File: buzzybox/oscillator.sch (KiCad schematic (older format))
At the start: 6 parts, among them Q1 Q_NPN_EBC

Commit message: complete mini layout
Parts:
- removed C2: C, Capacitor_THT:CP_Radial_D5.0mm_P2.50mm, symbol Device:C
- added C10: CP1, Capacitor_THT:CP_Radial_D4.0mm_P2.00mm, symbol Device:CP1
- Q1: value Q_NPN_EBC -> NPN
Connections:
- net at Q1.1 (E), R2.2, RV1.3: now also C10.1
- net at D1.2 (A), Q1.3 (C): now also C10.2
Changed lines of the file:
@@
 AR Path="/5FD4298B/5FB07025" Ref="Q14"  Part="1"
 F 0 "Q5" H 5641 3804 50  0000 L CNN
-F 1 "Q_NPN_EBC" H 5641 3895 50  0000 L CNN
+F 1 "NPN" H 5641 3895 50  0000 L CNN
 F 2 "buzzybox:TO-92-2" H 5650 3950 50  0001 C CNN
 F 3 "~" H 5450 3850 50  0001 C CNN
@@
 Wire Wire Line
 	5600 3550 5600 3650
-$Comp
-L Device:C C?
-U 1 1 5FB0704B
-P 5850 3850
-AR Path="/5FB0704B" Ref="C?"  Part="1"
-AR Path="/5FB04F5B/5FB0704B" Ref="C?"  Part="1"
-AR Path="/5FB0809B/5FB0704B" Ref="C?"  Part="1"
-AR Path="/5FB08189/5FB0704B" Ref="C?"  Part="1"
-AR Path="/5FB0823D/5FB0704B" Ref="C?"  Part="1"
-AR Path="/5FB0838F/5FB0704B" Ref="C?"  Part="1"
-AR Path="/5FB083E3/5FB0704B" Ref="C?"  Part="1"
-AR Path="/5FB084BD/5FB0704B" Ref="C?"  Part="1"
-AR Path="/5FB1B762/5FB0704B" Ref="C?"  Part="1"
-AR Path="/5FB1B962/5FB0704B" Ref="C?"  Part="1"
-AR Path="/5FB1BC8A/5FB0704B" Ref="C?"  Part="1"
-AR Path="/5FB1BF2A/5FB0704B" Ref="C?"  Part="1"
-AR Path="/5FB1C1D8/5FB0704B" Ref="C?"  Part="1"
-AR Path="/5FB1C552/5FB0704B" Ref="C?"  Part="1"
-AR Path="/5FD40CD3/5FB0704B" Ref="C2"  Part="1"
-AR Path="/5FD412A5/5FB0704B" Ref="C3"  Part="1"
-AR Path="/5FD41369/5FB0704B" Ref="C4"  Part="1"
-AR Path="/5FD41435/5FB0704B" Ref="C5"  Part="1"
-AR Path="/5FD4152B/5FB0704B" Ref="C6"  Part="1"
-AR Path="/5FD41635/5FB0704B" Ref="C7"  Part="1"
-AR Path="/5FD416C9/5FB0704B" Ref="C8"  Part="1"
-AR Path="/5FD42979/5FB0704B" Ref="C9"  Part="1"
-AR Path="/5FD4297C/5FB0704B" Ref="C10"  Part="1"
-AR Path="/5FD4297F/5FB0704B" Ref="C11"  Part="1"
-AR Path="/5FD42982/5FB0704B" Ref="C12"  Part="1"
-AR Path="/5FD42985/5FB0704B" Ref="C13"  Part="1"
-AR Path="/5FD42988/5FB0704B" Ref="C14"  Part="1"
-AR Path="/5FD4298B/5FB0704B" Ref="C15"  Part="1"
-F 0 "C6" H 5965 3896 50  0000 L CNN
-F 1 "C" H 5965 3805 50  0000 L CNN
-F 2 "Capacitor_THT:CP_Radial_D5.0mm_P2.50mm" H 5888 3700 50  0001 C CNN
-F 3 "~" H 5850 3850 50  0001 C CNN
-	1    5850 3850
-	1    0    0    -1
-$EndComp
 Wire Wire Line
 	5850 4050 5850 4000
@@
 	-1   0    0    1
 $EndComp
+$Comp
+L Device:CP1 C10
+U 1 1 5FD88ECD
+P 5850 3850
+AR Path="/5FD4297F/5FD88ECD" Ref="C10"  Part="1"
+AR Path="/5FD40CD3/5FD88ECD" Ref="C1"  Part="1"
+AR Path="/5FD412A5/5FD88ECD" Ref="C2"  Part="1"
+AR Path="/5FD41369/5FD88ECD" Ref="C3"  Part="1"
+AR Path="/5FD41435/5FD88ECD" Ref="C4"  Part="1"
+AR Path="/5FD4152B/5FD88ECD" Ref="C5"  Part="1"
+AR Path="/5FD41635/5FD88ECD" Ref="C6"  Part="1"
+AR Path="/5FD416C9/5FD88ECD" Ref="C7"  Part="1"
+AR Path="/5FD42979/5FD88ECD" Ref="C8"  Part="1"
+AR Path="/5FD4297C/5FD88ECD" Ref="C9"  Part="1"
+F 0 "C5" H 5965 3896 50  0000 L CNN
+F 1 "CP1" H 5965 3805 50  0000 L CNN
+F 2 "Capacitor_THT:CP_Radial_D4.0mm_P2.00mm" H 5850 3850 50  0001 C CNN
+F 3 "~" H 5850 3850 50  0001 C CNN
+	1    5850 3850
+	1    0    0    -1
+$EndComp
 $EndSCHEMATC

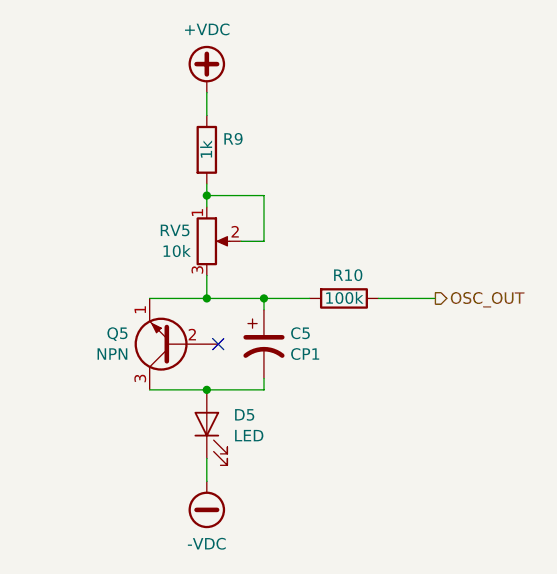
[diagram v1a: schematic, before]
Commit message: finalize main PCB after parts recieved
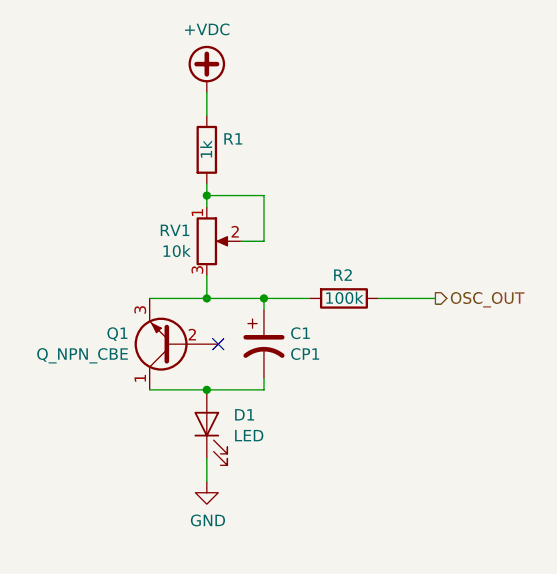
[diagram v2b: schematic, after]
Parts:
- removed Q1: NPN, buzzybox:TO-92-2, symbol Device:Q_NPN_EBC
- added Q1: Q_NPN_CBE, buzzybox:TO-92-2, symbol Device:Q_NPN_CBE
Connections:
- net at C10.1, R2.2, RV1.3: now also Q1.3 (E)
- net at C10.2, D1.2 (A): now also Q1.1 (C)
- net -VDC renamed GND
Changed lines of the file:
@@
 $Descr A4 11693 8268
 encoding utf-8
-Sheet 6 11
+Sheet 2 11
 Title ""
 Date ""
@@
 AR Path="/5FD42988/5FB07013" Ref="R25"  Part="1"
 AR Path="/5FD4298B/5FB07013" Ref="R27"  Part="1"
-F 0 "R9" H 5670 3046 50  0000 L CNN
+F 0 "R1" H 5670 3046 50  0000 L CNN
 F 1 "1k" V 5600 3000 50  0000 C CNN
 F 2 "Resistor_THT:R_Axial_DIN0207_L6.3mm_D2.5mm_P10.16mm_Horizontal" V 5530 3000 50  0001 C CNN
@@
 AR Path="/5FD42988/5FB07019" Ref="RV13"  Part="1"
 AR Path="/5FD4298B/5FB07019" Ref="RV14"  Part="1"
-F 0 "RV5" H 5530 3446 50  0000 R CNN
+F 0 "RV1" H 5530 3446 50  0000 R CNN
 F 1 "10k" H 5530 3355 50  0000 R CNN
 F 2 "Potentiometer_THT:Potentiometer_Alpha_RD901F-40-00D_Single_Vertical" H 5600 3400 50  0001 C CNN
@@
 AR Path="/5FD42988/5FB0701F" Ref="D13"  Part="1"
 AR Path="/5FD4298B/5FB0701F" Ref="D14"  Part="1"
-F 0 "D5" V 5639 4083 50  0000 R CNN
+F 0 "D1" V 5639 4083 50  0000 R CNN
 F 1 "LED" V 5548 4083 50  0000 R CNN
 F 2 "LED_THT:LED_D5.0mm" H 5600 4200 50  0001 C CNN
@@
 	1    5600 4200
 	0    -1   -1   0
-$EndComp
-$Comp
-L Device:Q_NPN_EBC Q?
-U 1 1 5FB07025
-P 5450 3850
-AR Path="/5FB07025" Ref="Q?"  Part="1"
-AR Path="/5FB04F5B/5FB07025" Ref="Q?"  Part="1"
-AR Path="/5FB0809B/5FB07025" Ref="Q?"  Part="1"
-AR Path="/5FB08189/5FB07025" Ref="Q?"  Part="1"
-AR Path="/5FB0823D/5FB07025" Ref="Q?"  Part="1"
-AR Path="/5FB0838F/5FB07025" Ref="Q?"  Part="1"
-AR Path="/5FB083E3/5FB07025" Ref="Q?"  Part="1"
-AR Path="/5FB084BD/5FB07025" Ref="Q?"  Part="1"
-AR Path="/5FB1B762/5FB07025" Ref="Q?"  Part="1"
-AR Path="/5FB1B962/5FB07025" Ref="Q?"  Part="1"
-AR Path="/5FB1BC8A/5FB07025" Ref="Q?"  Part="1"
-AR Path="/5FB1BF2A/5FB07025" Ref="Q?"  Part="1"
-AR Path="/5FB1C1D8/5FB07025" Ref="Q?"  Part="1"
-AR Path="/5FB1C552/5FB07025" Ref="Q?"  Part="1"
-AR Path="/5FD40CD3/5FB07025" Ref="Q1"  Part="1"
-AR Path="/5FD412A5/5FB07025" Ref="Q2"  Part="1"
-AR Path="/5FD41369/5FB07025" Ref="Q3"  Part="1"
-AR Path="/5FD41435/5FB07025" Ref="Q4"  Part="1"
-AR Path="/5FD4152B/5FB07025" Ref="Q5"  Part="1"
-AR Path="/5FD41635/5FB07025" Ref="Q6"  Part="1"
-AR Path="/5FD416C9/5FB07025" Ref="Q7"  Part="1"
-AR Path="/5FD42979/5FB07025" Ref="Q8"  Part="1"
-AR Path="/5FD4297C/5FB07025" Ref="Q9"  Part="1"
-AR Path="/5FD4297F/5FB07025" Ref="Q10"  Part="1"
-AR Path="/5FD42982/5FB07025" Ref="Q11"  Part="1"
-AR Path="/5FD42985/5FB07025" Ref="Q12"  Part="1"
-AR Path="/5FD42988/5FB07025" Ref="Q13"  Part="1"
-AR Path="/5FD4298B/5FB07025" Ref="Q14"  Part="1"
-F 0 "Q5" H 5641 3804 50  0000 L CNN
-F 1 "NPN" H 5641 3895 50  0000 L CNN
-F 2 "buzzybox:TO-92-2" H 5650 3950 50  0001 C CNN
-F 3 "~" H 5450 3850 50  0001 C CNN
-	1    5450 3850
-	-1   0    0    1
 $EndComp
 Wire Wire Line
@@
 AR Path="/5FD42988/5FB0703E" Ref="R26"  Part="1"
 AR Path="/5FD4298B/5FB0703E" Ref="R28"  Part="1"
-F 0 "R10" V 6100 3600 50  0000 L CNN
+F 0 "R2" V 6100 3600 50  0000 L CNN
 F 1 "100k" V 6200 3650 50  0000 C CNN
 F 2 "Resistor_THT:R_Axial_DIN0207_L6.3mm_D2.5mm_P10.16mm_Horizontal" V 6130 3650 50  0001 C CNN
@@
 AR Path="/5FD42988/5FD42DAA" Ref="#PWR0128"  Part="1"
 AR Path="/5FD4298B/5FD42DAA" Ref="#PWR0130"  Part="1"
-F 0 "#PWR0112" H 5600 2650 50  0001 C CNN
+F 0 "#PWR0104" H 5600 2650 50  0001 C CNN
 F 1 "+VDC" H 5600 3025 50  0000 C CNN
 F 2 "" H 5600 2750 50  0001 C CNN
@@
 	1    5600 2750
 	1    0    0    -1
-$EndComp
-$Comp
-L power:-VDC #PWR0105
-U 1 1 5FD43433
-P 5600 4450
-AR Path="/5FD40CD3/5FD43433" Ref="#PWR0105"  Part="1"
-AR Path="/5FD412A5/5FD43433" Ref="#PWR0107"  Part="1"
-AR Path="/5FD41369/5FD43433" Ref="#PWR0109"  Part="1"
-AR Path="/5FD41435/5FD43433" Ref="#PWR0111"  Part="1"
-AR Path="/5FD4152B/5FD43433" Ref="#PWR0113"  Part="1"
-AR Path="/5FD41635/5FD43433" Ref="#PWR0115"  Part="1"
-AR Path="/5FD416C9/5FD43433" Ref="#PWR0117"  Part="1"
-AR Path="/5FD42979/5FD43433" Ref="#PWR0119"  Part="1"
-AR Path="/5FD4297C/5FD43433" Ref="#PWR0121"  Part="1"
-AR Path="/5FD4297F/5FD43433" Ref="#PWR0123"  Part="1"
-AR Path="/5FD42982/5FD43433" Ref="#PWR0125"  Part="1"
-AR Path="/5FD42985/5FD43433" Ref="#PWR0127"  Part="1"
-AR Path="/5FD42988/5FD43433" Ref="#PWR0129"  Part="1"
-AR Path="/5FD4298B/5FD43433" Ref="#PWR0131"  Part="1"
-F 0 "#PWR0113" H 5600 4350 50  0001 C CNN
-F 1 "-VDC" H 5600 4725 50  0000 C CNN
-F 2 "" H 5600 4450 50  0001 C CNN
-F 3 "" H 5600 4450 50  0001 C CNN
-	1    5600 4450
-	-1   0    0    1
 $EndComp
 $Comp
@@
 AR Path="/5FD42979/5FD88ECD" Ref="C8"  Part="1"
 AR Path="/5FD4297C/5FD88ECD" Ref="C9"  Part="1"
-F 0 "C5" H 5965 3896 50  0000 L CNN
+F 0 "C1" H 5965 3896 50  0000 L CNN
 F 1 "CP1" H 5965 3805 50  0000 L CNN
 F 2 "Capacitor_THT:CP_Radial_D4.0mm_P2.00mm" H 5850 3850 50  0001 C CNN
@@
 	1    0    0    -1
 $EndComp
+$Comp
+L power:GND #PWR0109
+U 1 1 5FDA91C5
+P 5600 4450
+AR Path="/5FD40CD3/5FDA91C5" Ref="#PWR0109"  Part="1"
+AR Path="/5FD416C9/5FDA91C5" Ref="#PWR0121"  Part="1"
+AR Path="/5FD412A5/5FDA91C5" Ref="#PWR0111"  Part="1"
+AR Path="/5FD41369/5FDA91C5" Ref="#PWR0113"  Part="1"
+AR Path="/5FD41435/5FDA91C5" Ref="#PWR0115"  Part="1"
+AR Path="/5FD4152B/5FDA91C5" Ref="#PWR0117"  Part="1"
+AR Path="/5FD41635/5FDA91C5" Ref="#PWR0119"  Part="1"
+AR Path="/5FD42979/5FDA91C5" Ref="#PWR0123"  Part="1"
+AR Path="/5FD4297C/5FDA91C5" Ref="#PWR0124"  Part="1"
+AR Path="/5FD4297F/5FDA91C5" Ref="#PWR0126"  Part="1"
+F 0 "#PWR0109" H 5600 4200 50  0001 C CNN
+F 1 "GND" H 5605 4277 50  0000 C CNN
+F 2 "" H 5600 4450 50  0001 C CNN
+F 3 "" H 5600 4450 50  0001 C CNN
+	1    5600 4450
+	1    0    0    -1
+$EndComp
+$Comp
+L Device:Q_NPN_CBE Q1
+U 1 1 5FDA9F6B
+P 5450 3850
+AR Path="/5FD40CD3/5FDA9F6B" Ref="Q1"  Part="1"
+AR Path="/5FD412A5/5FDA9F6B" Ref="Q2"  Part="1"
+AR Path="/5FD41369/5FDA9F6B" Ref="Q3"  Part="1"
+AR Path="/5FD41435/5FDA9F6B" Ref="Q4"  Part="1"
+AR Path="/5FD4152B/5FDA9F6B" Ref="Q5"  Part="1"
+AR Path="/5FD41635/5FDA9F6B" Ref="Q6"  Part="1"
+AR Path="/5FD416C9/5FDA9F6B" Ref="Q7"  Part="1"
+AR Path="/5FD42979/5FDA9F6B" Ref="Q8"  Part="1"
+AR Path="/5FD4297C/5FDA9F6B" Ref="Q9"  Part="1"
+AR Path="/5FD4297F/5FDA9F6B" Ref="Q10"  Part="1"
+F 0 "Q1" H 5641 3804 50  0000 L CNN
+F 1 "Q_NPN_CBE" H 5641 3895 50  0000 L CNN
+F 2 "buzzybox:TO-92-2" H 5650 3950 50  0001 C CNN
+F 3 "~" H 5450 3850 50  0001 C CNN
+	1    5450 3850
+	-1   0    0    1
+$EndComp
 $EndSCHEMATC
